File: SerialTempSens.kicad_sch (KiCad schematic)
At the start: 35 parts, among them J1 Conn_01x02, J2 Conn_01x02, J3 Conn_01x02, J4 USB_B_Micro, J5 Conn_01x05, SW1 SW_Push, U1 MIC5504-3.3YM5, U2 STM32G0B1KCTx, U3 OLED Display, U4 USBLC6-2SC6

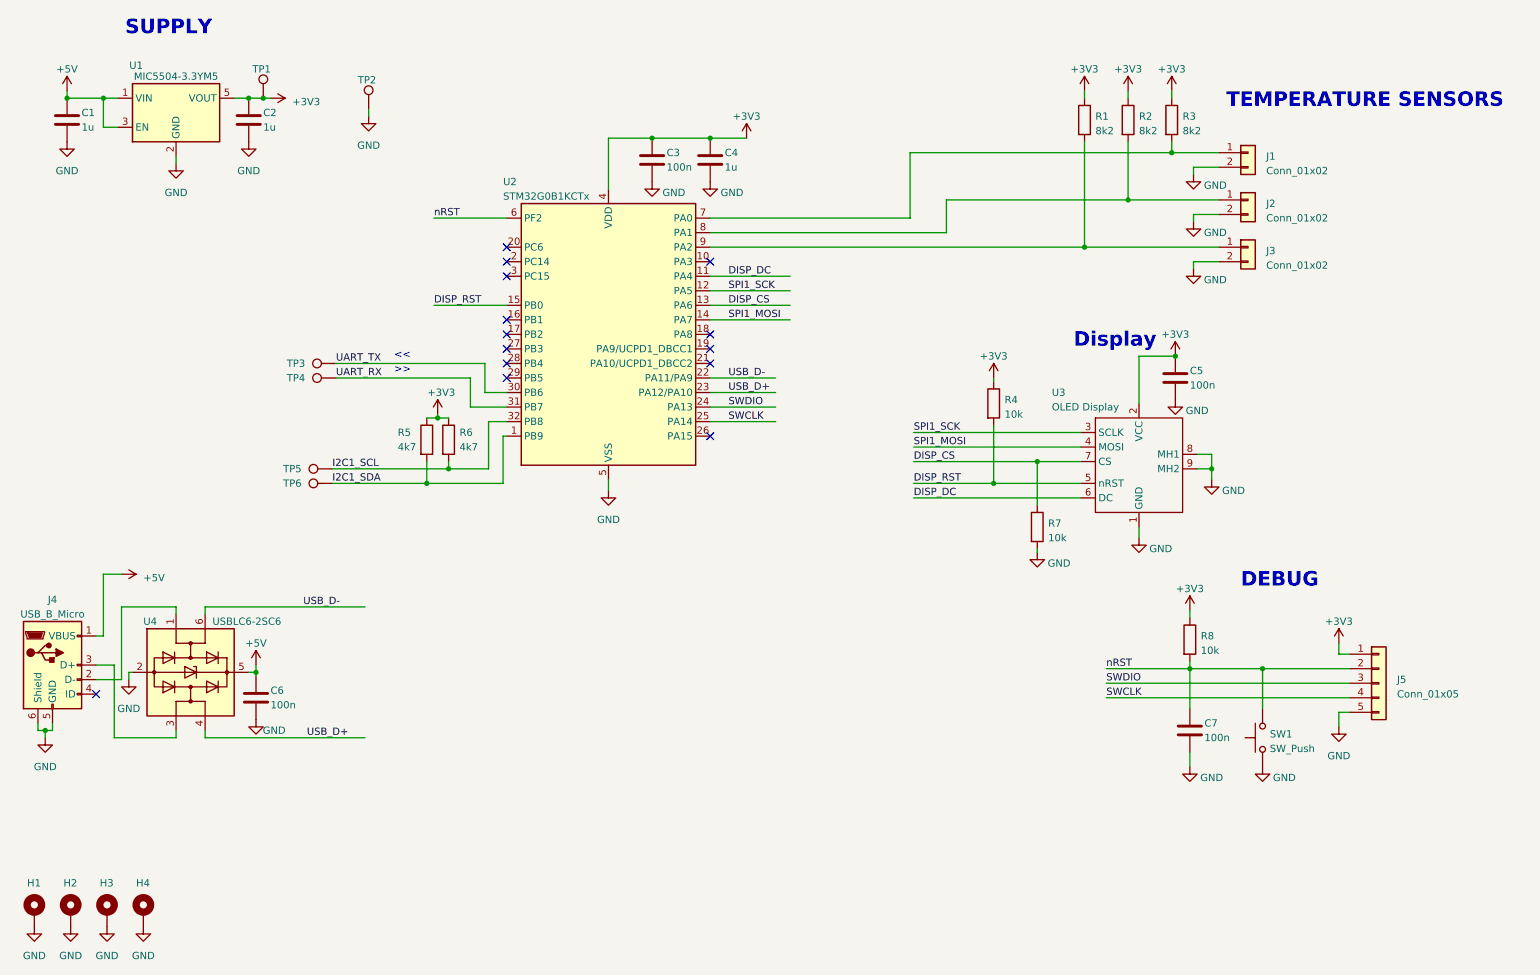
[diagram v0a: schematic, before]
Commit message: Rename project, update footprint
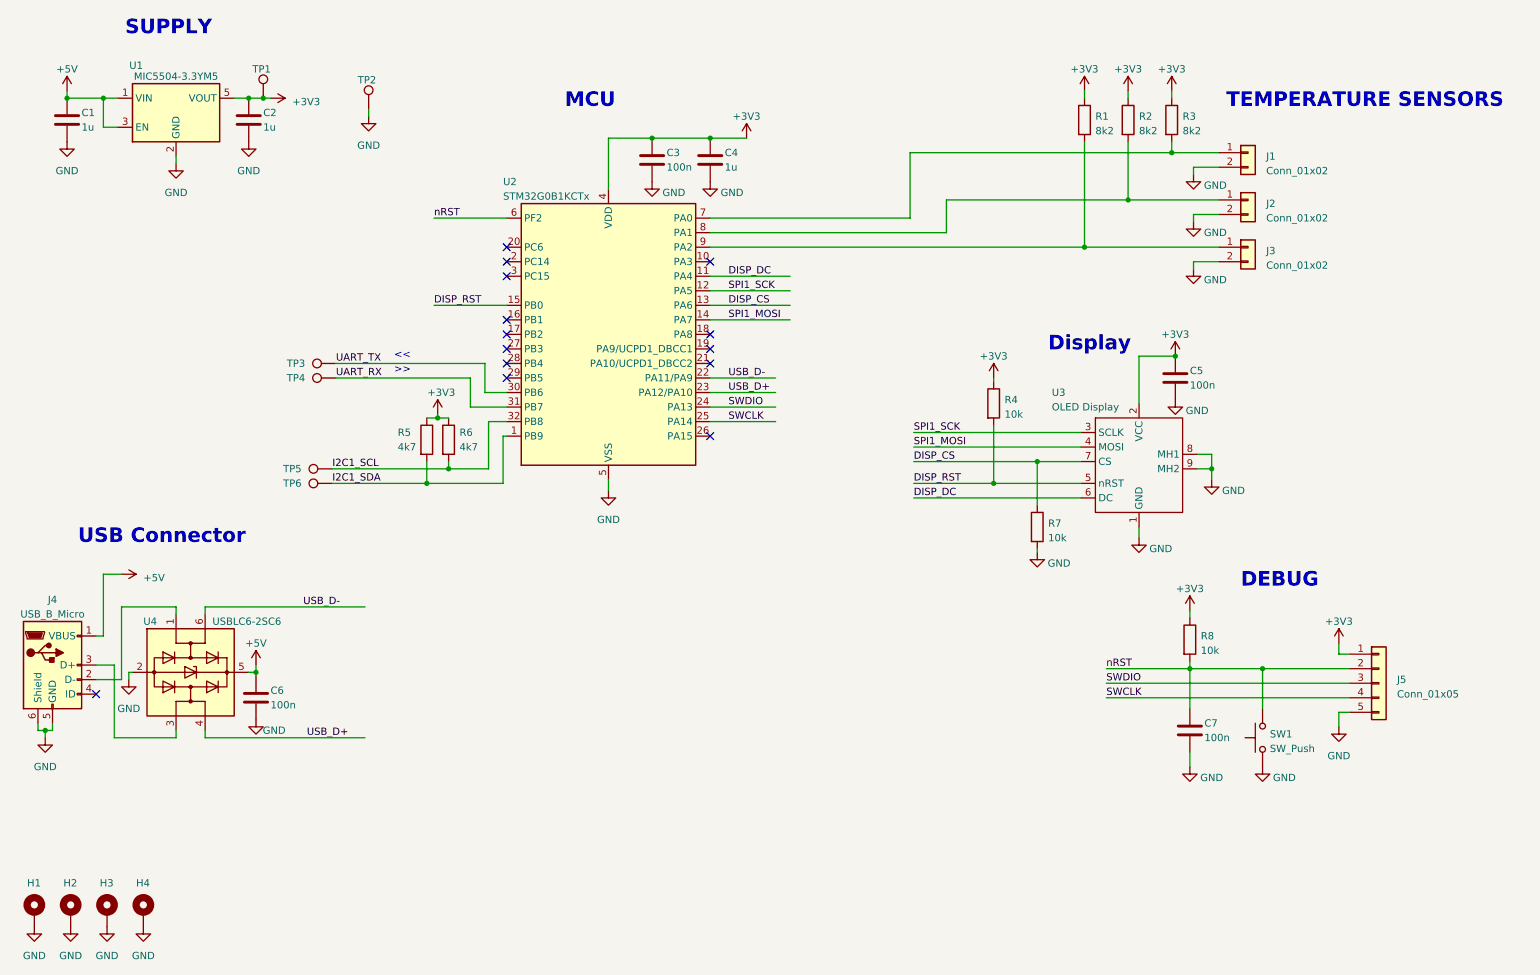
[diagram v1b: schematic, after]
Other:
- note added: "MCU"
- note added: "USB Connector"
